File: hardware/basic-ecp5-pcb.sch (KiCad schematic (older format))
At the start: 62 parts, among them J1 Conn_01x02, J2 Conn_02x20_Odd_Even, J3 Conn_02x06_Odd_Even, J4 Conn_02x06_Odd_Even, J5 Conn_02x06_Odd_Even, J6 Conn_02x06_Odd_Even, J7 Conn_02x06_Odd_Even, J8 Conn_02x06_Odd_Even, J9 Conn_02x20_Odd_Even, Q1 Q_NMOS_GSD, SW1 SW_Push, SW2 SW_Push, U2 IS25LP016D-JBLE, U3 TLV73311PDBV, U4 TLV73333PDBV, U5 TLV73325PDBV, X1 SiT2001B

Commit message: changes for design review (see readme)
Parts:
- removed C23, C24, C25: 100n, Capacitor_SMD:C_0805_2012Metric, symbol Device:C
- removed L1, L4: L, Inductor_SMD:L_0805_2012Metric, symbol Device:L
- removed TP7: 3.3v, TestPoint:TestPoint_THTPad_D1.0mm_Drill0.5mm, symbol Connector:TestPoint
- removed U3: TLV73311PDBV, Package_TO_SOT_SMD:SOT-23-5, symbol Regulator_Linear:TLV73312PDBV
- removed U4: TLV73333PDBV, Package_TO_SOT_SMD:SOT-23-5, symbol Regulator_Linear:TLV73333PDBV
- added C9: 100n, Capacitor_SMD:C_0805_2012Metric, symbol Device:C
- added FB1, FB2, FB3: Ferrite_Bead_Small, Inductor_SMD:L_0805_2012Metric, symbol Device:Ferrite_Bead_Small
- added R4: 100k, Resistor_SMD:R_0805_2012Metric, symbol Device:R
- added R5: 120k, Resistor_SMD:R_0805_2012Metric, symbol Device:R
- added R7: 68k, Resistor_SMD:R_0805_2012Metric, symbol Device:R
- added R8: 15k, Resistor_SMD:R_0805_2012Metric, symbol Device:R
- added TP1: 3.3v, TestPoint:TestPoint_THTPad_D1.0mm_Drill0.5mm, symbol Connector:TestPoint
- added U3, U4: TLV62568DBV, Package_TO_SOT_SMD:SOT-23-5, symbol Regulator_Switching:TLV62568DBV
- C11, C26, C7: value 100n -> 10u
- C12, C13: value 1u -> 4.7u
- C14: value 1u -> 22u
- C15: value 1u -> 10u
- L2, L3: value L -> 2.2uH; footprint Inductor_SMD:L_0805_2012Metric -> Inductor_SMD:L_Taiyo-Yuden_NR-40xx
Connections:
- net +3V3 is gone; now on net +3.3VP: C1.1, C2.1, C4.1, C5.1, C6.1, C7.1, D1.2 (A), L3.2, R1.1, R10.2, R11.2, R12.2, R13.2, R2.1, U2.8 (VCC), X1.3 (OE), X1.4 (Vcc)
- net 2v5 is gone; now on net +2V5: C20.1, U5.5 (OUT)
- net +1V1: now also C14.1, C9.1, R4.2
- net +3.3VP: now also C15.1, R7.2, TP1.1
- net +5V: now also FB1.2, FB2.2, FB3.2; no longer C12.1, C13.1, C3.1, U5.1 (IN), U5.3 (EN)
- net GND: now also C9.2, R5.1, R8.1, U3.2 (GND), U4.2 (GND)
- net 1v1: no longer names the net of L2.1
- net 1v1: now also U3.3 (SW); no longer C14.1
- net 3v3: no longer names the net of L3.1
- net 3v3: now also U4.3 (SW); no longer C15.1
- new net: C12.1, FB1.1, U3.1 (EN), U3.4 (VIN)
- new net: C3.1, FB3.1, U5.1 (IN), U5.3 (EN)
- new net: R4.1, R5.2, U3.5 (FB)
- new net: C13.1, FB2.1, U4.1 (EN), U4.4 (VIN)
- new net: R7.1, R8.2, U4.5 (FB)
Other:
- note added: "1.1v @ 1A\n"
- note added: "3.3v @ 1A\n"
- note removed: "1.1v @ 300mA"
- note removed: "3.3v @ 300mA"
- moved on the sheet: C12, C14, TP6

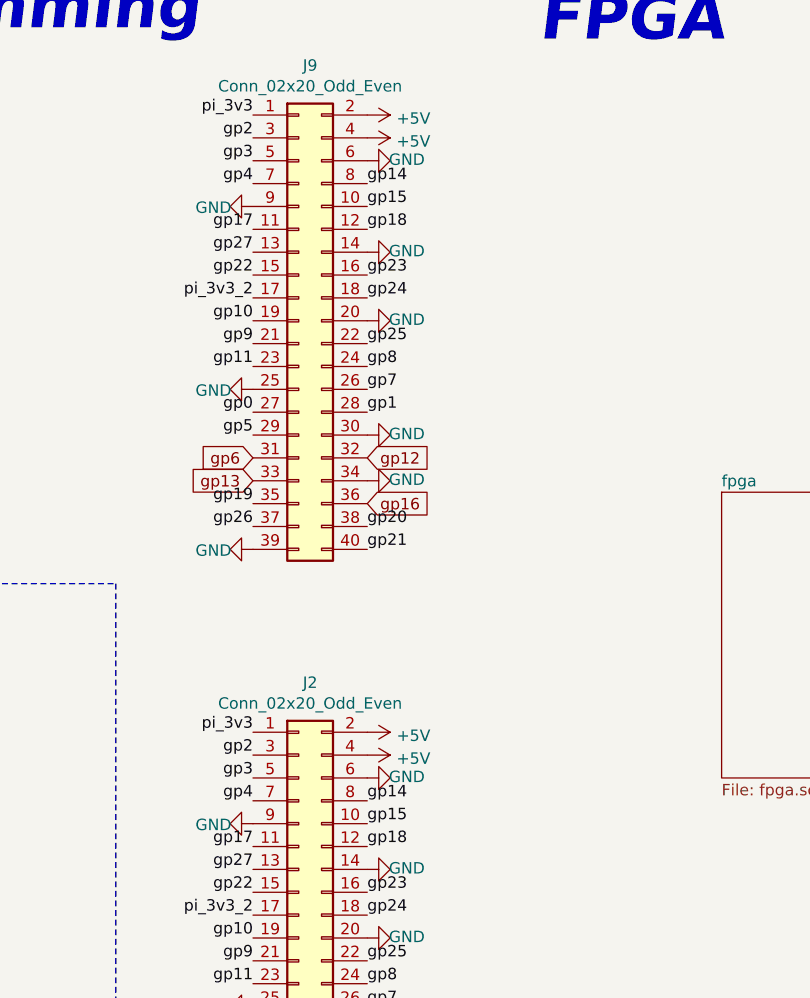
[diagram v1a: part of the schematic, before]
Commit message: add serial connection
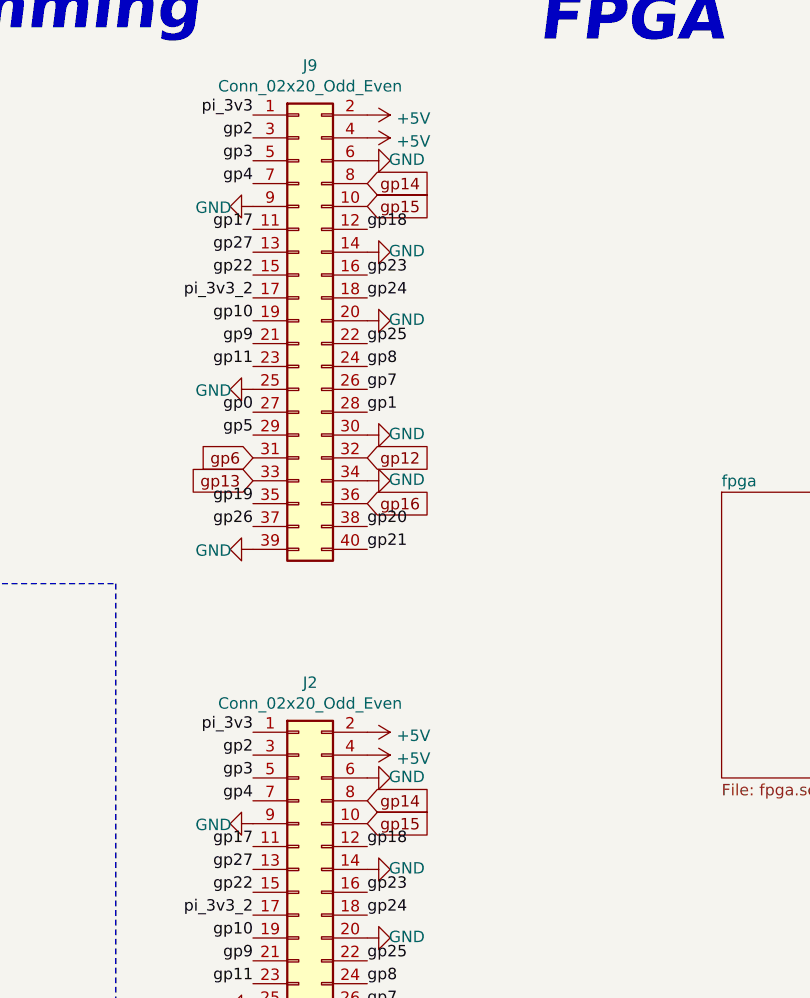
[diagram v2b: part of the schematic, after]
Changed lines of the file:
@@
 EndData
 $EndBitmap
-Text Label 6000 4200 0    50   ~ 0
-gp14
-Text Label 6000 4300 0    50   ~ 0
-gp15
 Text Label 6000 4400 0    50   ~ 0
 gp18
@@
 	0    1    1    0
 $EndComp
-Text Label 6000 6900 0    50   ~ 0
-gp14
-Text Label 6000 7000 0    50   ~ 0
-gp15
 Text Label 6000 7100 0    50   ~ 0
 gp18
@@
 	1150 1800 1400 1800
 Connection ~ 1400 1800
+Text GLabel 6000 4200 2    50   Input ~ 0
+gp14
+Text GLabel 6000 4300 2    50   Input ~ 0
+gp15
+Text GLabel 6000 7000 2    50   Input ~ 0
+gp15
+Text GLabel 6000 6900 2    50   Input ~ 0
+gp14
 $EndSCHEMATC

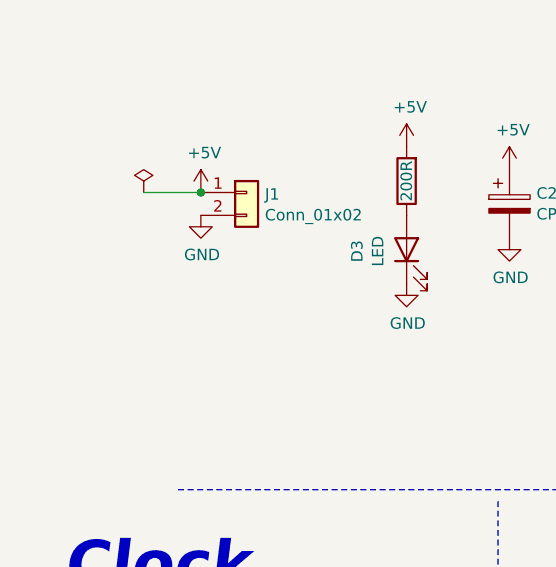
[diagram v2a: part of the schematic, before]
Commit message: added input R for dc/dc
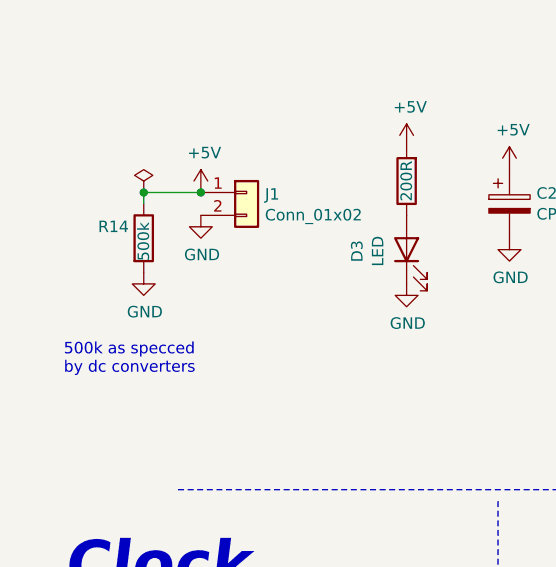
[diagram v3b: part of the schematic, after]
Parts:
- added R14: 500k, Resistor_SMD:R_0805_2012Metric, symbol Device:R
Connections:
- net +5V: now also R14.1
- net GND: now also R14.2
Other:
- note added: "500k as specced\nby dc converters"
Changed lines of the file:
@@
 Text GLabel 6000 6900 2    50   Input ~ 0
 gp14
+$Comp
+L Device:R R14
+U 1 1 5F15DC38
+P 1150 2000
+F 0 "R14" H 950 2050 50  0000 L CNN
+F 1 "500k" V 1150 1900 50  0000 L CNN
+F 2 "Resistor_SMD:R_0805_2012Metric" V 1080 2000 50  0001 C CNN
+F 3 "~" H 1150 2000 50  0001 C CNN
+	1    1150 2000
+	1    0    0    -1
+$EndComp
+$Comp
+L power:GND #PWR0106
+U 1 1 5F15E1E2
+P 1150 2150
+F 0 "#PWR0106" H 1150 1900 50  0001 C CNN
+F 1 "GND" H 1155 1977 50  0000 C CNN
+F 2 "" H 1150 2150 50  0001 C CNN
+F 3 "" H 1150 2150 50  0001 C CNN
+	1    1150 2150
+	1    0    0    -1
+$EndComp
+Wire Wire Line
+	1150 1850 1150 1800
+Connection ~ 1150 1800
+Text Notes 800  2600 0    50   ~ 0
+500k as specced\nby dc converters
 $EndSCHEMATC

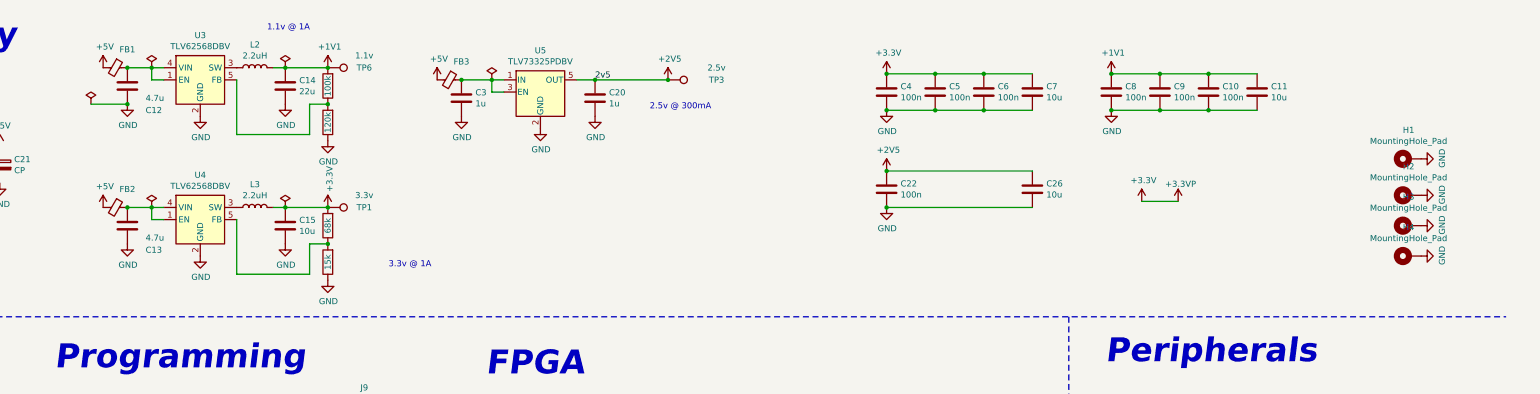
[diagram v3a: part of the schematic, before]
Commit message: part numbers and notes on dc/dc voltage dividers
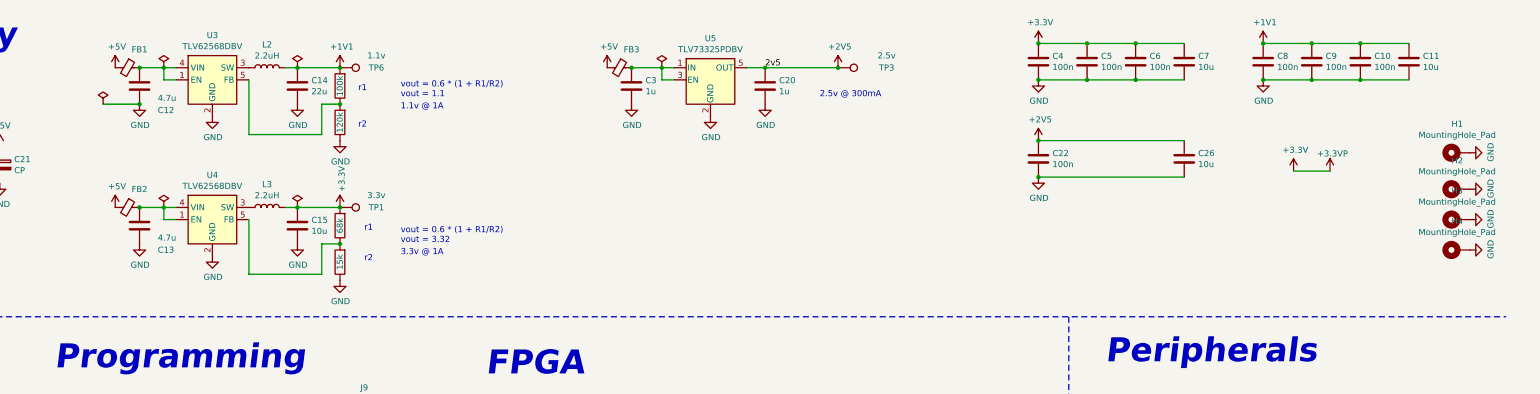
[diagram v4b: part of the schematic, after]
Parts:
- C11, C15, C26, C7: manf# (none) -> ‎C0805C106K8PACTU‎
- C12, C13: manf# (none) -> C0805C475K9PACTU
- C14: manf# (none) -> C0805C226M9PACTU
- C20, C3: manf# (none) -> C0805C105Z4VACTU
- L2, L3: manf# (none) -> SDER041H-2R2MS
- Q1: manf# (none) -> DMG1012UW-7
- R1, R10, R11, R2: manf# (none) -> RC0805FR-0710KL
- R12, R13, R6, R9: manf# (none) -> RC0805FR-07200RL
- R4: manf# (none) -> RC0805FR-07100KL
- R5: manf# (none) -> RC0805FR-07120KL
- R7: manf# (none) -> RC0805FR-0768KL
- R8: manf# (none) -> RC0805FR-0715KL
- U2: manf# (none) -> IS25LP016D-JBLE-TR‎
- U3, U4: manf# (none) -> TLV62568PDDCT‎
- U5: manf# (none) -> TLV73325PDBVR‎
- X1: manf# (none) -> SIT2001BI-S2-33N-16.000000G‎
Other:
- note added: "r1"
- note added: "r2"
- note added: "vout = 0.6 * (1 + R1/R2)\nvout = 1.1"
- note added: "vout = 0.6 * (1 + R1/R2)\nvout = 3.32"
- moved on the sheet: C10, C11, C12, C13, C14, C15, C20, C22, C26, C3, C4, C5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

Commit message: fix wrong package version of switcher chip
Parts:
- U3, U4: manf# TLV62568PDDCT‎ -> TLV62568DBVT
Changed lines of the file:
@@
 F 2 "Package_TO_SOT_SMD:SOT-23-5" H 4550 900 50  0001 L CIN
 F 3 "http://www.ti.com/lit/ds/symlink/tlv62568.pdf" H 4250 1600 50  0001 C CNN
-F 4 "TLV62568PDDCT‎" H 4500 1150 50  0001 C CNN "manf#"
+F 4 "TLV62568DBVT" H 4500 1150 50  0001 C CNN "manf#"
 	1    4500 1150
 	1    0    0    -1
@@
 F 2 "Package_TO_SOT_SMD:SOT-23-5" H 4550 2050 50  0001 L CIN
 F 3 "http://www.ti.com/lit/ds/symlink/tlv62568.pdf" H 4250 2750 50  0001 C CNN
-F 4 "TLV62568PDDCT‎" H 4500 2300 50  0001 C CNN "manf#"
+F 4 "TLV62568DBVT" H 4500 2300 50  0001 C CNN "manf#"
 	1    4500 2300
 	1    0    0    -1

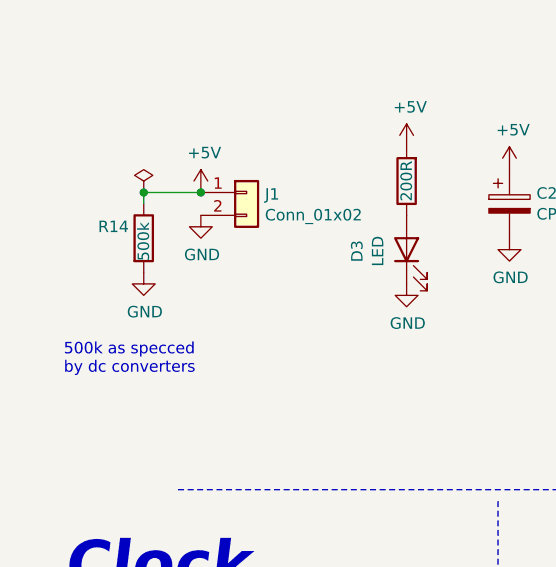
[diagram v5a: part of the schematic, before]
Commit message: removed unneeded pullup for PG pin on buck converters
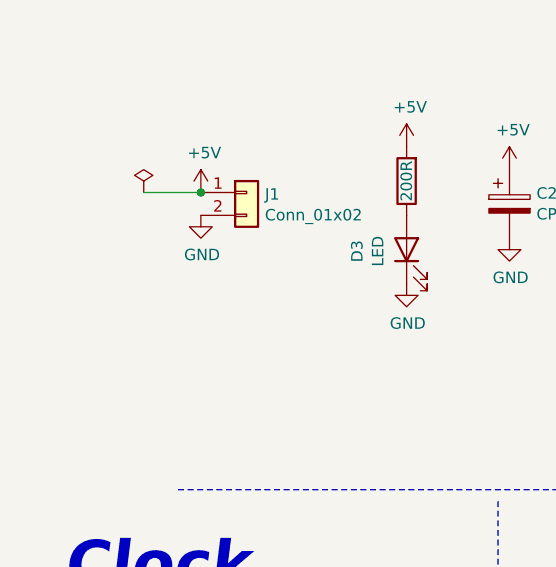
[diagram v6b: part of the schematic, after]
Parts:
- removed R14: 500k, Resistor_SMD:R_0805_2012Metric, symbol Device:R
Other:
- note removed: "500k as specced\nby dc converters"
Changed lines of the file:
@@
 Text GLabel 6000 6900 2    50   Input ~ 0
 gp14
-$Comp
-L Device:R R14
-U 1 1 5F15DC38
-P 1150 2000
-F 0 "R14" H 950 2050 50  0000 L CNN
-F 1 "500k" V 1150 1900 50  0000 L CNN
-F 2 "Resistor_SMD:R_0805_2012Metric" V 1080 2000 50  0001 C CNN
-F 3 "~" H 1150 2000 50  0001 C CNN
-	1    1150 2000
-	1    0    0    -1
-$EndComp
-$Comp
-L power:GND #PWR0106
-U 1 1 5F15E1E2
-P 1150 2150
-F 0 "#PWR0106" H 1150 1900 50  0001 C CNN
-F 1 "GND" H 1155 1977 50  0000 C CNN
-F 2 "" H 1150 2150 50  0001 C CNN
-F 3 "" H 1150 2150 50  0001 C CNN
-	1    1150 2150
-	1    0    0    -1
-$EndComp
-Wire Wire Line
-	1150 1850 1150 1800
-Connection ~ 1150 1800
-Text Notes 800  2600 0    50   ~ 0
-500k as specced\nby dc converters
 Text Notes 5700 1250 0    50   ~ 0
 r1

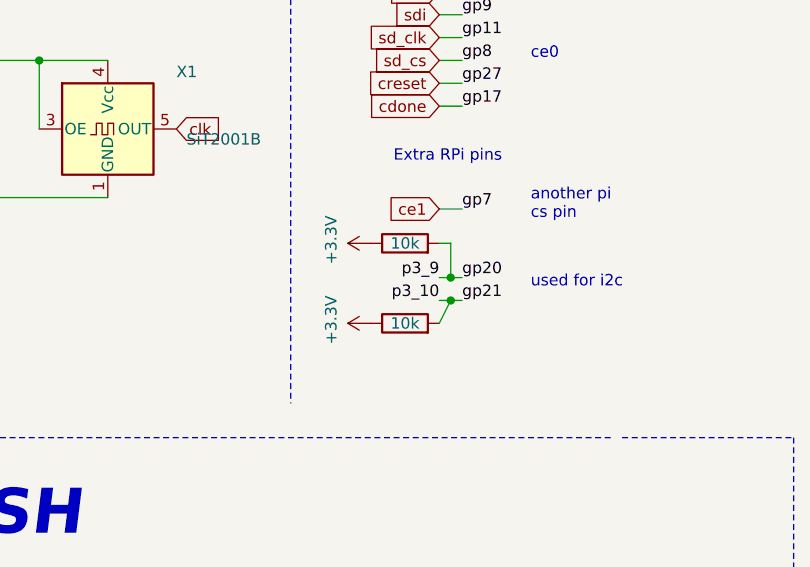
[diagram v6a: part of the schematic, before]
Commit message: change 10k i2c pullups to 4k7
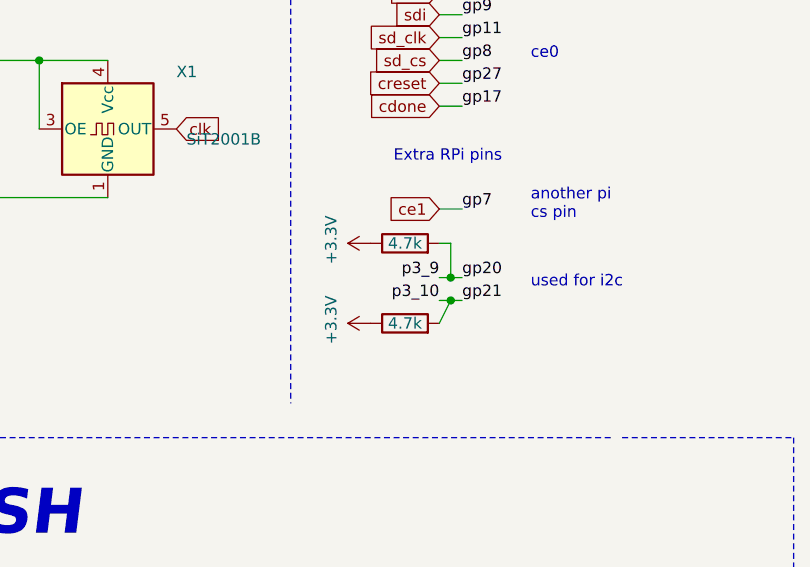
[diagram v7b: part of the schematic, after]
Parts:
- R1, R2: value 10k -> 4.7k
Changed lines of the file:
@@
 P 3200 5100
 F 0 "R1" V 2993 5100 50  0001 C CNN
-F 1 "10k" V 3200 5100 50  0000 C CNN
+F 1 "4.7k" V 3200 5100 50  0000 C CNN
 F 2 "Resistor_SMD:R_0805_2012Metric" V 3130 5100 50  0001 C CNN
 F 3 "~" H 3200 5100 50  0001 C CNN
@@
 P 3200 5450
 F 0 "R2" V 2993 5450 50  0001 C CNN
-F 1 "10k" V 3200 5450 50  0000 C CNN
+F 1 "4.7k" V 3200 5450 50  0000 C CNN
 F 2 "Resistor_SMD:R_0805_2012Metric" V 3130 5450 50  0001 C CNN
 F 3 "~" H 3200 5450 50  0001 C CNN
